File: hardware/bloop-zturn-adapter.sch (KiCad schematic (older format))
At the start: 3 parts, among them J2 Z-Turn CN2, P2 BLOOP SPI CONTROL, P3 BLOOP SPI CONTROL

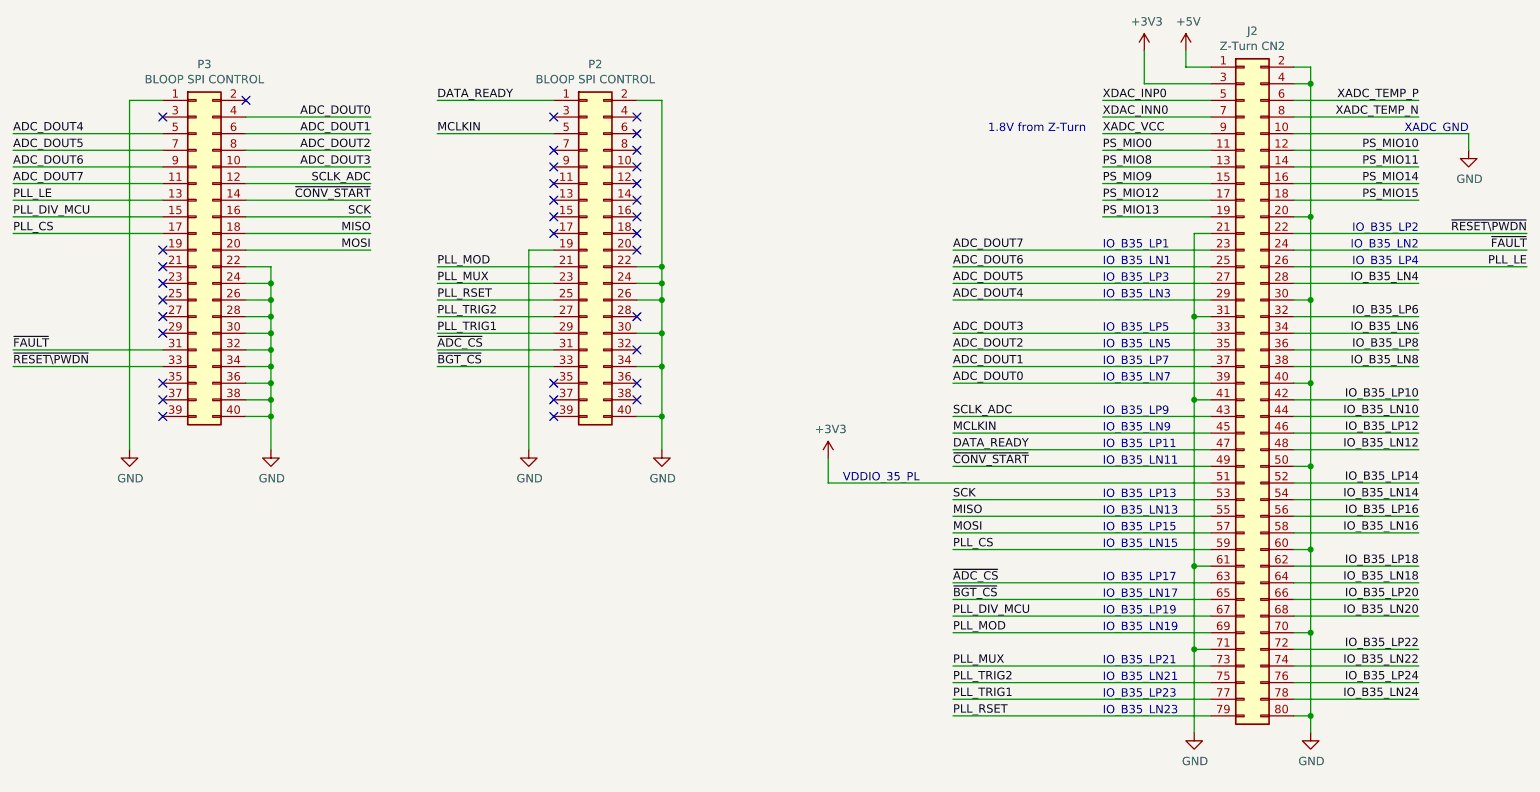
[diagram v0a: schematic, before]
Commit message: Schematic edits to make layout routing easier and completed layout. Generated gerbers and pdf schematic.
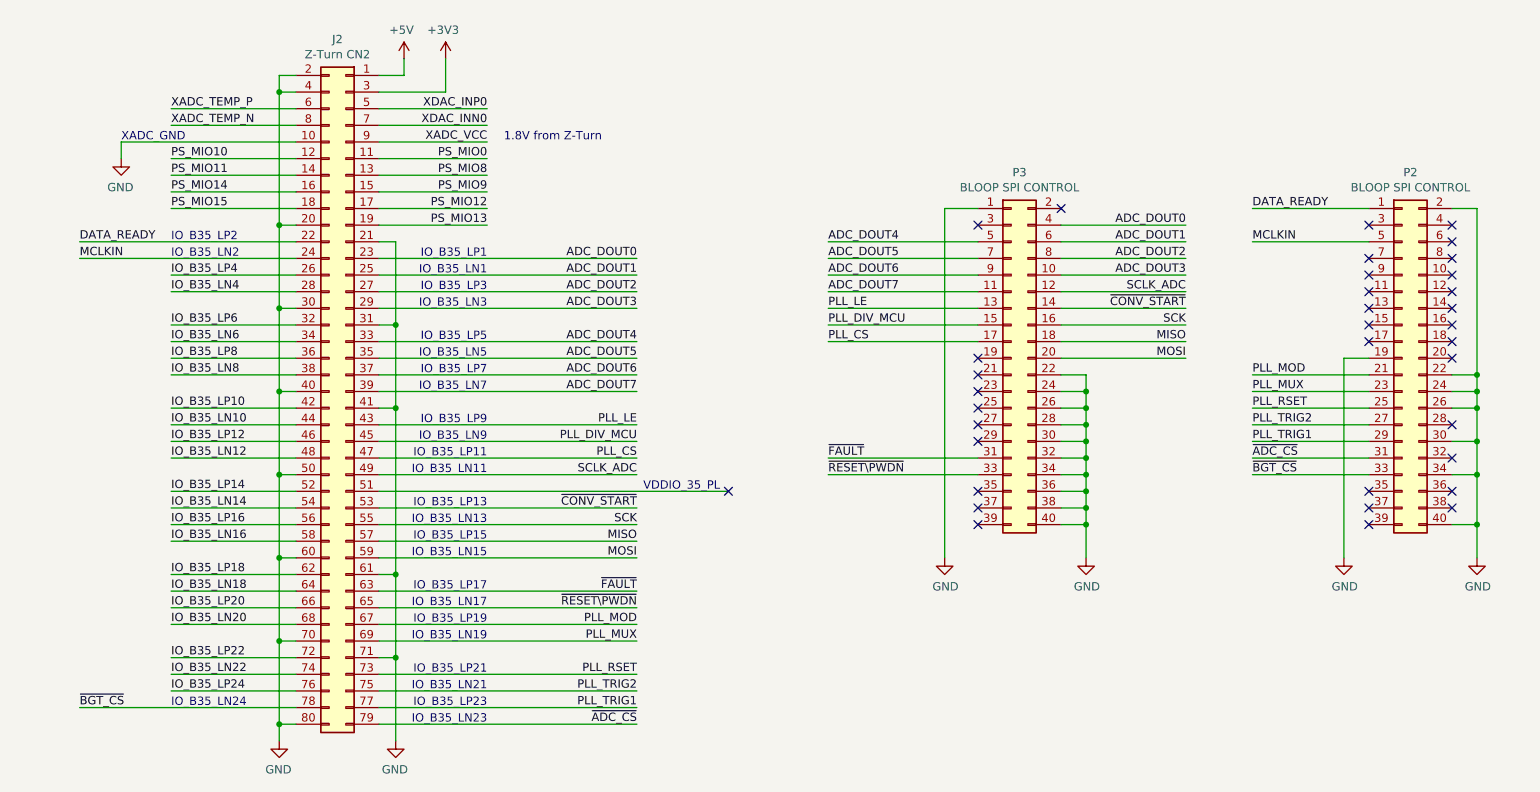
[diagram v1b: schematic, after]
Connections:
- net IO_B35_LN24 is gone; now on net ~BGT_CS: J2.78 (Pin_78)
- net +3V3: no longer J2.51 (Pin_51)
- net ADC_DOUT0: now also J2.23 (Pin_23); no longer J2.39 (Pin_39)
- net ADC_DOUT1: now also J2.25 (Pin_25); no longer J2.37 (Pin_37)
- net ADC_DOUT2: now also J2.27 (Pin_27); no longer J2.35 (Pin_35)
- net ADC_DOUT3: now also J2.29 (Pin_29); no longer J2.33 (Pin_33)
- net ADC_DOUT4: now also J2.33 (Pin_33); no longer J2.29 (Pin_29)
- net ADC_DOUT5: now also J2.35 (Pin_35); no longer J2.27 (Pin_27)
- net ADC_DOUT6: now also J2.37 (Pin_37); no longer J2.25 (Pin_25)
- net ADC_DOUT7: now also J2.39 (Pin_39); no longer J2.23 (Pin_23)
- net DATA_READY: now also J2.22 (Pin_22); no longer J2.47 (Pin_47)
- net MCLKIN: now also J2.24 (Pin_24); no longer J2.45 (Pin_45)
- net MISO: now also J2.57 (Pin_57); no longer J2.55 (Pin_55)
- net MOSI: now also J2.59 (Pin_59); no longer J2.57 (Pin_57)
- net PLL_CS: now also J2.47 (Pin_47); no longer J2.59 (Pin_59)
- net PLL_DIV_MCU: now also J2.45 (Pin_45); no longer J2.67 (Pin_67)
- net PLL_LE: now also J2.43 (Pin_43); no longer J2.26 (Pin_26)
- net PLL_MOD: now also J2.67 (Pin_67); no longer J2.69 (Pin_69)
- net PLL_MUX: now also J2.69 (Pin_69); no longer J2.73 (Pin_73)
- net PLL_RSET: now also J2.73 (Pin_73); no longer J2.79 (Pin_79)
- net SCK: now also J2.55 (Pin_55); no longer J2.53 (Pin_53)
- net SCLK_ADC: now also J2.49 (Pin_49); no longer J2.43 (Pin_43)
- net ~ADC_CS: now also J2.79 (Pin_79); no longer J2.63 (Pin_63)
- net ~BGT_CS: no longer J2.65 (Pin_65)
- net ~CONV_START: now also J2.53 (Pin_53); no longer J2.49 (Pin_49)
- net ~FAULT: now also J2.63 (Pin_63); no longer J2.24 (Pin_24)
- net ~RESET\PWDN: now also J2.65 (Pin_65); no longer J2.22 (Pin_22)
- new net IO_B35_LP4: J2.26 (Pin_26)
- no-connect marks 34 -> 35
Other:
- note added: "IO_B35_LN24"
- note removed: "IO_B35_LP4"
- moved on the sheet: J2, P2, P3

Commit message: Generated BOM
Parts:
- P2, P3: MPN (none) -> 95157-140LF
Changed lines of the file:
@@
 F 1 "BLOOP SPI CONTROL" H 7250 4426 50  0000 C CNN
 F 2 "Connector_PinHeader_2.54mm:PinHeader_2x20_P2.54mm_Vertical_SMD" H 7200 3400 50  0001 C CNN
-F 3 "~" H 7200 3400 50  0001 C CNN
+F 3 "https://cdn.amphenol-icc.com/media/wysiwyg/files/drawing/95157.pdf" H 7200 3400 50  0001 C CNN
+F 4 "95157-140LF" H 7200 3400 50  0001 C CNN "MPN"
 	1    7200 3400
 	1    0    0    -1
@@
 F 1 "BLOOP SPI CONTROL" H 9600 4426 50  0000 C CNN
 F 2 "Connector_PinHeader_2.54mm:PinHeader_2x20_P2.54mm_Vertical_SMD" H 9550 3400 50  0001 C CNN
-F 3 "~" H 9550 3400 50  0001 C CNN
+F 3 "https://cdn.amphenol-icc.com/media/wysiwyg/files/drawing/95157.pdf" H 9550 3400 50  0001 C CNN
+F 4 "95157-140LF" H 9550 3400 50  0001 C CNN "MPN"
 	1    9550 3400
 	1    0    0    -1
